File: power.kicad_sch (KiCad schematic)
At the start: 13 parts, among them J1 Conn_01x02_Socket, U1 TPS61170DRVR

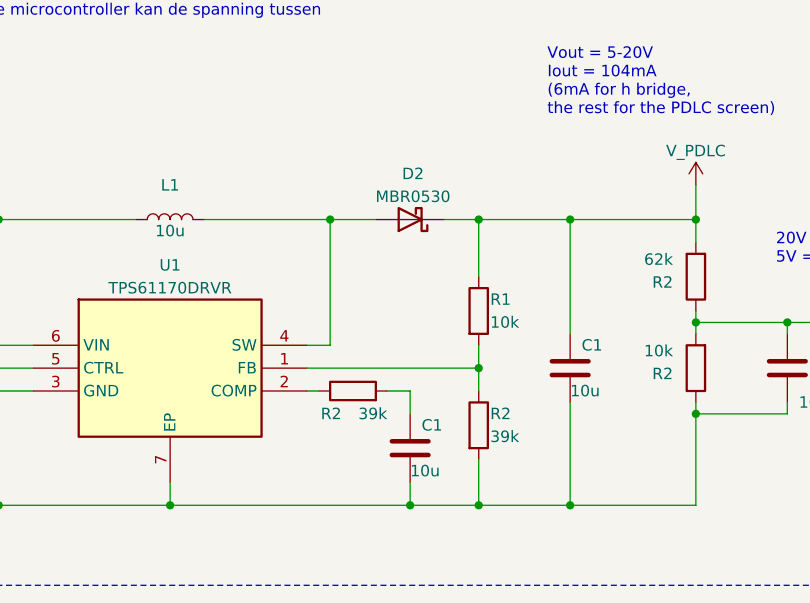
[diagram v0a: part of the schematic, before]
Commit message: Buffed the diode, changed compensation components
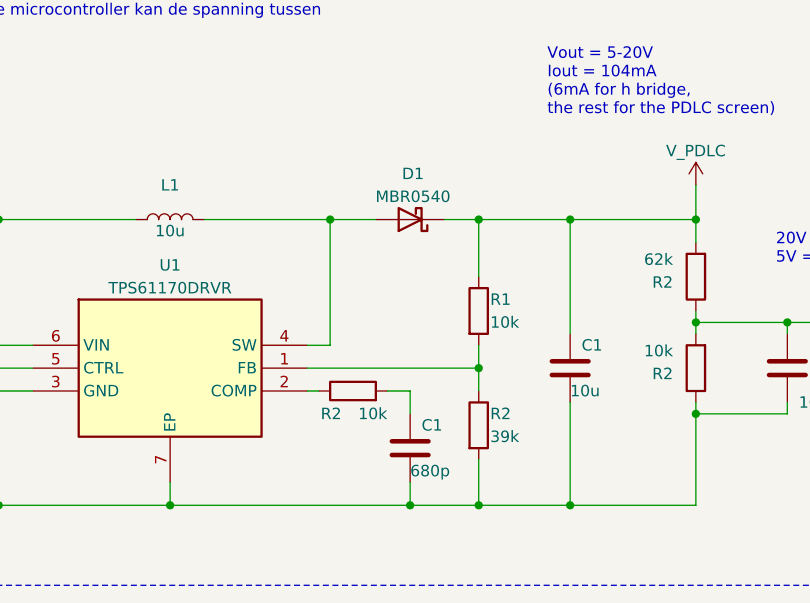
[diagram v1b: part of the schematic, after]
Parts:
- removed D2: MBR0530, Diode_SMD:D_SOD-123, symbol Diode:MBR0530
- added D1: MBR0540, Diode_SMD:D_SOD-123, symbol Diode:MBR0540
- C1: value 10u -> 680p
- R2: value 39k -> 10k
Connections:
- net VCC: now also D1.1 (K)
- net at L1.1, U1.4 (SW): now also D1.2 (A)
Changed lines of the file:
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@@
       (effects (font (size 1.27 1.27)) (justify left))
     )
-    (property "Value" "39k" (at 217.17 69.85 90)
+    (property "Value" "10k" (at 217.17 69.85 90)
       (effects (font (size 1.27 1.27)) (justify left))
     )
@@
       (effects (font (size 1.27 1.27)) (justify left))
     )
-    (property "Value" "10u" (at 219.71 76.2 0)
+    (property "Value" "680p" (at 219.71 76.2 0)
       (effects (font (size 1.27 1.27)) (justify left))
     )
@@
     )
   )
-  (symbol (lib_id "Diode:MBR0530") (at 219.71 48.26 180) (unit 1)
-    (in_bom yes) (on_board yes) (dnp no) (fields_autoplaced)
-    (property "Reference" "D2" (at 220.0275 43.18 0)
-      (effects (font (size 1.27 1.27)))
-    )
-    (property "Value" "MBR0530" (at 220.0275 45.72 0)
+  (symbol (lib_id "Diode:MBR0540") (at 219.71 48.26 180) (unit 1)
+    (in_bom yes) (on_board yes) (dnp no) (fields_autoplaced)
+    (property "Reference" "D1" (at 220.0275 43.18 0)
+      (effects (font (size 1.27 1.27)))
+    )
+    (property "Value" "MBR0540" (at 220.0275 45.72 0)
       (effects (font (size 1.27 1.27)))
     )
@@
       (project "RookBril"
         (path "/5dc439a9-720d-4bdc-b61f-78a76fde4df5/2d26b15a-54d8-4f7d-a410-dc25ffe321a1"
-          (reference "D2") (unit 1)
-        )
-      )
+          (reference "D1") (unit 1)
+        )
+      )

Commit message: updated schematic
alles toegevoegd aan de schematic
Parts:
- removed J1: Conn_01x02_Socket, symbol Connector:Conn_01x02_Socket
- renumbered C1 to C?, L1 to L?, R2 to R?, R1 to R?, U1 to U3
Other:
- note removed: "0.8-1.5V/cell 3 cell 2.4-4.5V totaal"
- note removed: "3V Buck-Boost"
- note removed: "Een simpele ldo is niet goed want dat zorgt ervoor dat de pwm voltage niet constant blijft en daardoor is de pdlc output voltage niet constant"
- moved on the sheet: C?, D1, L?, R?, U3

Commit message: footprint assignments gedaan + verbeteringen
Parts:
- removed L?: 10u, symbol Device:L
- added L1: VLCF5020T-100M1R1-1, VLCF5020, symbol SamacSys_Parts:VLCF5020T-100M1R1-1
- C? (x4): footprint (none) -> Capacitor_SMD:C_0805_2012Metric_Pad1.18x1.45mm_HandSolder
- renumbered U3 to U2
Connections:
- net +BATT: now also L1.1
- net at D1.2 (A), U2.4 (SW): now also L1.2
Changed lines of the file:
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@@
   (junction (at 206.375 107.315) (diameter 0) (color 0 0 0 0)
   )
+  (junction (at 155.575 95.885) (diameter 0) (color 0 0 0 0)
+  )
   (junction (at 196.215 117.475) (diameter 0) (color 0 0 0 0)
   )
@@
   )
   (junction (at 196.215 95.885) (diameter 0) (color 0 0 0 0)
-  )
-  (junction (at 155.575 95.885) (diameter 0) (color 0 0 0 0)
   )
   (junction (at 172.085 95.885) (diameter 0) (color 0 0 0 0)
@@
     (stroke (width 0) (type dash))
   )
-  (wire (pts (xy 141.605 95.885) (xy 155.575 95.885))
-    (stroke (width 0) (type default))
-  )
-  (wire (pts (xy 118.745 95.885) (xy 133.985 95.885))
-    (stroke (width 0) (type default))
-  )
   (wire (pts (xy 172.085 112.395) (xy 172.085 114.935))
     (stroke (width 0) (type default))
@@
     (stroke (width 0) (type dash))
   )
+  (wire (pts (xy 118.745 95.885) (xy 127 95.885))
+    (stroke (width 0) (type default))
+  )
   (wire (pts (xy 155.575 95.885) (xy 155.575 109.855))
     (stroke (width 0) (type default))
@@
   )
   (wire (pts (xy 164.465 127.635) (xy 172.085 127.635))
+    (stroke (width 0) (type default))
+  )
+  (wire (pts (xy 147.32 95.885) (xy 155.575 95.885))
     (stroke (width 0) (type default))
   )
@@
         )
         (path "/5dc439a9-720d-4bdc-b61f-78a76fde4df5/2d26b15a-54d8-4f7d-a410-dc25ffe321a1"
-          (reference "R8") (unit 1)
+          (reference "R12") (unit 1)
         )
       )
@@
       (effects (font (size 1.27 1.27)) (justify left))
     )
-    (property "Footprint" "" (at 183.2102 116.205 0)
+    (property "Footprint" "Capacitor_SMD:C_0805_2012Metric_Pad1.18x1.45mm_HandSolder" (at 183.2102 116.205 0)
       (effects (font (size 1.27 1.27)) hide)
     )
@@
         )
         (path "/5dc439a9-720d-4bdc-b61f-78a76fde4df5/2d26b15a-54d8-4f7d-a410-dc25ffe321a1"
-          (reference "C11") (unit 1)
+          (reference "C7") (unit 1)
         )
       )
@@
   (symbol (lib_id "CustomSymbols:V_PDLC") (at 196.215 92.075 0) (unit 1)
     (in_bom yes) (on_board yes) (dnp no) (fields_autoplaced)
-    (property "Reference" "#PWR036" (at 196.215 95.885 0)
+    (property "Reference" "#PWR027" (at 196.215 95.885 0)
       (effects (font (size 1.27 1.27)) hide)
     )
@@
       (project "RookBril"
         (path "/5dc439a9-720d-4bdc-b61f-78a76fde4df5/2d26b15a-54d8-4f7d-a410-dc25ffe321a1"
-          (reference "#PWR036") (unit 1)
-        )
-      )
-    )
-  )
-  (symbol (lib_id "Device:L") (at 137.795 95.885 270) (mirror x) (unit 1)
-    (in_bom yes) (on_board yes) (dnp no)
-    (property "Reference" "L?" (at 137.795 92.075 90)
-      (effects (font (size 1.27 1.27)))
-    )
-    (property "Value" "10u" (at 137.795 97.155 90)
-      (effects (font (size 1.27 1.27)))
-    )
-    (property "Footprint" "" (at 137.795 95.885 0)
-      (effects (font (size 1.27 1.27)) hide)
-    )
-    (property "Datasheet" "~" (at 137.795 95.885 0)
-      (effects (font (size 1.27 1.27)) hide)
-    )
-    (pin "1")
-    (pin "2")
-    (instances
-      (project "RookBril"
-        (path "/5dc439a9-720d-4bdc-b61f-78a76fde4df5"
-          (reference "L?") (unit 1)
-        )
-        (path "/5dc439a9-720d-4bdc-b61f-78a76fde4df5/2d26b15a-54d8-4f7d-a410-dc25ffe321a1"
-          (reference "L1") (unit 1)
+          (reference "#PWR027") (unit 1)
         )
       )
@@
   (symbol (lib_id "power:GND") (at 102.235 128.905 0) (unit 1)
     (in_bom yes) (on_board yes) (dnp no) (fields_autoplaced)
-    (property "Reference" "#PWR038" (at 102.235 135.255 0)
+    (property "Reference" "#PWR029" (at 102.235 135.255 0)
       (effects (font (size 1.27 1.27)) hide)
     )
@@
       (project "RookBril"
         (path "/5dc439a9-720d-4bdc-b61f-78a76fde4df5/2d26b15a-54d8-4f7d-a410-dc25ffe321a1"
-          (reference "#PWR038") (unit 1)
+          (reference "#PWR029") (unit 1)
         )
       )
@@
         )
         (path "/5dc439a9-720d-4bdc-b61f-78a76fde4df5/2d26b15a-54d8-4f7d-a410-dc25ffe321a1"
-          (reference "R4") (unit 1)
+          (reference "R8") (unit 1)
         )
       )
@@
       (effects (font (size 1.27 1.27)) (justify left))
     )
-    (property "Footprint" "" (at 103.2002 113.665 0)
+    (property "Footprint" "Capacitor_SMD:C_0805_2012Metric_Pad1.18x1.45mm_HandSolder" (at 103.2002 113.665 0)
       (effects (font (size 1.27 1.27)) hide)
     )
@@
         )
         (path "/5dc439a9-720d-4bdc-b61f-78a76fde4df5/2d26b15a-54d8-4f7d-a410-dc25ffe321a1"
-          (reference "C10") (unit 1)
+          (reference "C6") (unit 1)
         )
       )
@@
         )
         (path "/5dc439a9-720d-4bdc-b61f-78a76fde4df5/2d26b15a-54d8-4f7d-a410-dc25ffe321a1"
-          (reference "R7") (unit 1)
+          (reference "R11") (unit 1)
         )
       )
@@
   (symbol (lib_id "power:+BATT") (at 102.235 93.345 0) (unit 1)
     (in_bom yes) (on_board yes) (dnp no) (fields_autoplaced)
-    (property "Reference" "#PWR037" (at 102.235 97.155 0)
+    (property "Reference" "#PWR028" (at 102.235 97.155 0)
       (effects (font (size 1.27 1.27)) hide)
     )
@@
       (project "RookBril"
         (path "/5dc439a9-720d-4bdc-b61f-78a76fde4df5/2d26b15a-54d8-4f7d-a410-dc25ffe321a1"
-          (reference "#PWR037") (unit 1)
+          (reference "#PWR028") (unit 1)
         )
       )
@@
         )
         (path "/5dc439a9-720d-4bdc-b61f-78a76fde4df5/2d26b15a-54d8-4f7d-a410-dc25ffe321a1"
-          (reference "R6") (unit 1)
+          (reference "R10") (unit 1)
         )
       )
@@
       (effects (font (size 1.27 1.27)) (justify left))
     )
-    (property "Footprint" "" (at 207.3402 116.205 0)
+    (property "Footprint" "Capacitor_SMD:C_0805_2012Metric_Pad1.18x1.45mm_HandSolder" (at 207.3402 116.205 0)
       (effects (font (size 1.27 1.27)) hide)
     )
@@
         )
         (path "/5dc439a9-720d-4bdc-b61f-78a76fde4df5/2d26b15a-54d8-4f7d-a410-dc25ffe321a1"
-          (reference "C12") (unit 1)
+          (reference "C8") (unit 1)
         )
       )
@@
         )
         (path "/5dc439a9-720d-4bdc-b61f-78a76fde4df5/2d26b15a-54d8-4f7d-a410-dc25ffe321a1"
-          (reference "R5") (unit 1)
+          (reference "R9") (unit 1)
         )
       )
@@
       (effects (font (size 1.27 1.27)) (justify left))
     )
-    (property "Footprint" "" (at 165.4302 125.095 0)
+    (property "Footprint" "Capacitor_SMD:C_0805_2012Metric_Pad1.18x1.45mm_HandSolder" (at 165.4302 125.095 0)
       (effects (font (size 1.27 1.27)) hide)
     )
@@
         )
         (path "/5dc439a9-720d-4bdc-b61f-78a76fde4df5/2d26b15a-54d8-4f7d-a410-dc25ffe321a1"
-          (reference "C13") (unit 1)
+          (reference "C9") (unit 1)
         )
       )
@@
     )
   )
+  (symbol (lib_id "SamacSys_Parts:VLCF5020T-100M1R1-1") (at 127 95.885 0) (unit 1)
+    (in_bom yes) (on_board yes) (dnp no) (fields_autoplaced)
+    (property "Reference" "L1" (at 137.16 90.17 0)
+      (effects (font (size 1.27 1.27)))
+    )
+    (property "Value" "VLCF5020T-100M1R1-1" (at 137.16 92.71 0)
+      (effects (font (size 1.27 1.27)))
+    )
+    (property "Footprint" "VLCF5020" (at 143.51 94.615 0)
+      (effects (font (size 1.27 1.27)) (justify left) hide)
+    )
+    (property "Datasheet" "https://product.tdk.com/system/files/dam/doc/product/inductor/inductor/smd/catalog/inductor_commercial_power_vlcf5020-1_en.pdf" (at 143.51 97.155 0)
+      (effects (font (size 1.27 1.27)) (justify left) hide)
+    )
+    (property "Description" "TDK VLC5020 Series Shielded Wire-wound SMD Inductor 10 uH +/-20% 1.5A Idc" (at 143.51 99.695 0)
+      (effects (font (size 1.27 1.27)) (justify left) hide)
+    )
+    (property "Height" "" (at 143.51 102.235 0)
+      (effects (font (size 1.27 1.27)) (justify left) hide)
+    )
+    (property "Mouser Part Number" "810-VLCF52T100M1R11" (at 143.51 104.775 0)
+      (effects (font (size 1.27 1.27)) (justify left) hide)
+    )
+    (property "Mouser Price/Stock" "https://www.mouser.co.uk/ProductDetail/TDK/VLCF5020T-100M1R1-1?qs=O2qRfqcg9D93TlFS8ggxKg%3D%3D" (at 143.51 107.315 0)
+      (effects (font (size 1.27 1.27)) (justify left) hide)
+    )
+    (property "Manufacturer_Name" "TDK" (at 143.51 109.855 0)
+      (effects (font (size 1.27 1.27)) (justify left) hide)
+    )
+    (property "Manufacturer_Part_Number" "VLCF5020T-100M1R1-1" (at 143.51 112.395 0)
+      (effects (font (size 1.27 1.27)) (justify left) hide)
+    )
+    (pin "1")
+    (pin "2")
+    (instances
+      (project "RookBril"
+        (path "/5dc439a9-720d-4bdc-b61f-78a76fde4df5/2d26b15a-54d8-4f7d-a410-dc25ffe321a1"
+          (reference "L1") (unit 1)
+        )
+      )
+    )
+  )
   (symbol (lib_id "CustomSymbols:TPS61170DRVR") (at 122.555 107.315 0) (unit 1)
     (in_bom yes) (on_board yes) (dnp no) (fields_autoplaced)
-    (property "Reference" "U3" (at 137.795 100.965 0)
+    (property "Reference" "U2" (at 137.795 100.965 0)
       (effects (font (size 1.27 1.27)))
     )
@@
       (project "RookBril"
         (path "/5dc439a9-720d-4bdc-b61f-78a76fde4df5/2d26b15a-54d8-4f7d-a410-dc25ffe321a1"
-          (reference "U3") (unit 1)
-        )
-      )
+          (reference "U2") (unit 1)
+        )
+      )

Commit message: aantal componenten veranderd.
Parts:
- removed L1: VLCF5020T-100M1R1-1, VLCF5020, symbol SamacSys_Parts:VLCF5020T-100M1R1-1
- added L1: VLCF5020T-100M1R1-1, Components:VLCF5020, symbol CustomSymbols:VLCF5020T-100M1R1-1
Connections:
- net +BATT: now also L1.1
- net at D1.2 (A), U2.4 (SW): now also L1.2

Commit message: nieuwe layout
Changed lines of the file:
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@@
     (effects (font (size 1.27 1.27)) (justify left bottom))
   )
-  (text "Vin_min = 3.2V\nVin_max = 6V" (at 113.665 84.455 0)
+  (text "Vin_min = 3.2V\nVin_max = 6V" (at 113.792 84.582 0)
     (effects (font (size 1.27 1.27)) (justify right bottom))
   )

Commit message: NieuwePDLCVoedingen
-LT1308
-LT3759
-Mixed schematic
-Mixed footprints
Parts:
- added C001, C19: 680p, symbol Device:C
- added C1301, C25: 100n, symbol Device:C
- added C26: 33u, symbol Device:C_Polarized
- added C27: 22n, symbol Device:C
- added C28, C3701: 50n, symbol Device:C
- added C29, C3702: 4.7u, symbol Device:C
- added C30: 10u, symbol Device:C
- added D01, D1301, D1302, D2, D3, D4, D5: ~, symbol CustomSymbols:MBRS140
- added L001, L3, L4: 4.7u, symbol Device:L
- added Q01, Q02, Q03, Q04, Q1, Q2, Q3, Q371, Q4, Q5, Q6, Q7, Q8, Q9: NMOS, symbol Simulation_SPICE:NMOS
- added R009, R30: 590k, symbol Device:R
- added R010, R19, R35: 47.6k, symbol Device:R
- added R011, R21, R31: 160k, symbol Device:R
- added R012, R22, R32: 80k, symbol Device:R
- added R013, R23, R33: 40k, symbol Device:R
- added R014, R24, R34: 20k, symbol Device:R
- added R1301, R1304 (x2), R3704, R3705, R3707: 0, symbol Device:R
- added R1302, R18, R27, R3701, R3706: 100k, symbol Device:R
- added R1303, R3703: 10k, symbol Device:R
- added R20: 300k, symbol Device:R
- added R25, R36: 5m, symbol Device:R
- added R26: 41.2k, symbol Device:R
- added R28: 118k, symbol Device:R
- added R29: 105k, symbol Device:R
- added U5: ~, symbol CustomSymbols:LT1308BCS8
- added U6: ~, symbol CustomSymbols:LT3759
- added U7: ~, symbol CustomSymbols:MixLT1308+LT3759
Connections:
- net +BATT: now also L3.1, L4.1, R29.1, U5.3 (SHDN), U5.6 (Vin), U6.11 (Vin)
- net GND: now also C001.2, C19.2, C26.2, C27.1, C28.1, C29.1, C30.1, C3701.1, C3702.1, Q01.3 (S), Q02.3 (S), Q03.3 (S), Q04.3 (S), Q1.3 (S), Q2.3 (S), Q3.3 (S), Q4.3 (S), Q6.3 (S), Q7.3 (S), Q8.3 (S), Q9.3 (S), R010.1, R1303.1, R19.1, R25.1, R26.2, R28.2, R35.1, R36.1, R3701.1, R3703.2, R3706.1, U5.4 (GND), U6.13 (GND), U7.15 (GND), U7.7 (X/GND)
- net vout_fb: now also C26.1, D4.1 (K), D5.1 (K), R20.2, R30.2, U6.10 (DRIVE)
- new net: C28.2, U6.3 (SS)
- new net: Q8.1 (D), R33.1
- new net: R30.1, R31.2, R32.2, R33.2, R34.2, R35.2, U6.2 (FBX)
- new net: Q2.1 (D), R22.1
- new net: R19.2, R20.1, R21.2, R22.2, R23.2, R24.2, U5.2 (FB)
- new net: Q7.1 (D), R32.1
- new net: C29.2, R27.1, U6.9 (INTVcc)
- new net: C25.2, D3.1 (K), D4.2 (A)
- new net: C30.2, D2.1 (K), D3.2 (A)
- new net: Q3.1 (D), R23.1
- new net: D01.1 (K), R009.2, R3704.1
- new net: C1301.2, D01.2 (A), D1301.1 (K), R3705.2
- new net: Q9.1 (D), R34.1
- new net: D5.2 (A), L4.2, Q5.1 (D)
- new net: C3701.2, R1301.1, U7.3 (SS/FB)
- new net: R009.1, R010.2, R011.2, R012.2, R013.2, R014.2, R1301.2, U7.2 (FBX/X)
- new net: R28.1, R29.2, U6. (Vc)
- new net: Q1.1 (D), R21.1
- new net: C1301.1, D1302.2 (A), L001.1, Q371.1 (D), R3705.1, U7.8 (X/SW)
- new net: R3701.2, U7.4 (RT/X)
- new net: Q371.2 (G), R1304.1, U7.10 (GATE/Vin)
- new net: L001.2, R1304.2, U7.13 (Vin/X)
- new net: R1302.2, U7.1 (Vc/Vc)
- new net: C3702.2, U7.11 (INTVcc/X)
- new net: R3704.2, U7.12 (DRIVE/LBI)
- new net: R3707.2, U7.14 (EN-UVLO/LBO)
- new net: R1304.1, U7.5 (SYNC/SHDN)
- new net: R3706.2, U7.6 (PGOOD/X)
- new net: Q371.3 (S), R36.2, U7.9 (SENSE/X)
- new net: C25.1, D2.2 (A), L3.2, U5.5 (SW)
- new net: Q03.1 (D), R013.1
- new net: Q5.3 (S), R25.2, U6.7 (SENSE)
- new net: R26.1, U6.4 (RT)
- new net: Q04.1 (D), R014.1
- new net: Q4.1 (D), R24.1
- new net: D1301.2 (A), D1302.1 (K)
- new net: C001.1, R1302.1
- new net: R27.2, U6.6 (PGOOD)
- new net: Q6.1 (D), R31.1
- new net: C27.2, U6. (Vc)
- new net: R18.2, U5.1 (Vcc)
- new net: Q5.2 (G), U6.8 (GATE)
- new net: Q01.1 (D), R011.1
- new net: C19.1, R18.1
- new net: Q02.1 (D), R012.1
- new net pdlc_bit0: Q01.2 (G), Q1.2 (G), Q3.2 (G), Q6.2 (G)
- new net pdlc_bit1: Q02.2 (G), Q2.2 (G), Q4.2 (G), Q7.2 (G)
- new net pdlc_bit2: Q03.2 (G), Q8.2 (G)
- new net pdlc_bit3: Q04.2 (G), Q9.2 (G)
- new net vout_EN: R1303.2, R1304.2, R3703.1, R3707.1
- no-connect marks 0 -> 3
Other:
- moved on the sheet: C?, D1, L1, R?, U2

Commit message: PCBv2.01
Eerste versie van de tweede versie van de pcb prototype.
Nieuwe PDLC voeding, extra pinnen beschikbaar voor GUI inclusief voeding pinnen.
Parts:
- removed C001: 680p, symbol Device:C
- removed C1301: 100n, symbol Device:C
- removed C26: 33u, symbol Device:C_Polarized
- removed C30: 10u, symbol Device:C
- removed C3701: 50n, symbol Device:C
- removed C3702: 4.7u, symbol Device:C
- removed C? (x2): 10u, Capacitor_SMD:C_0805_2012Metric_Pad1.18x1.45mm_HandSolder, symbol Device:C
- removed C?: 100n, Capacitor_SMD:C_0805_2012Metric_Pad1.18x1.45mm_HandSolder, symbol Device:C
- removed C?: 680p, Capacitor_SMD:C_0805_2012Metric_Pad1.18x1.45mm_HandSolder, symbol Device:C
- removed D01, D1301, D1302, D4: ~, symbol CustomSymbols:MBRS140
- removed D1: MBR0540, Diode_SMD:D_SOD-123, symbol Diode:MBR0540
- removed L001, L3: 4.7u, symbol Device:L
- removed L1: VLCF5020T-100M1R1-1, Components:VLCF5020, symbol CustomSymbols:VLCF5020T-100M1R1-1
- removed Q01, Q02, Q03, Q04, Q1, Q2, Q3, Q371, Q4: NMOS, symbol Simulation_SPICE:NMOS
- removed R009: 590k, symbol Device:R
- removed R010, R19: 47.6k, symbol Device:R
- removed R011, R21: 160k, symbol Device:R
- removed R012, R22: 80k, symbol Device:R
- removed R013, R23: 40k, symbol Device:R
- removed R014, R24: 20k, symbol Device:R
- removed R1301, R1304 (x2), R3704, R3705, R3707: 0, symbol Device:R
- removed R1302, R18, R3701, R3706: 100k, symbol Device:R
- removed R1303, R3703: 10k, symbol Device:R
- removed R20: 300k, symbol Device:R
- removed R29: 105k, symbol Device:R
- removed R36: 5m, symbol Device:R
- removed R?: 39k, Resistor_SMD:R_0805_2012Metric_Pad1.20x1.40mm_HandSolder, symbol Device:R
- removed R?: 62k, Resistor_SMD:R_0805_2012Metric_Pad1.20x1.40mm_HandSolder, symbol Device:R
- removed R? (x3): 10k, Resistor_SMD:R_0805_2012Metric_Pad1.20x1.40mm_HandSolder, symbol Device:R
- removed U2: TPS61170DRVR, Components:SON65P200X200X80-7N, symbol CustomSymbols:TPS61170DRVR
- removed U5: ~, symbol CustomSymbols:LT1308BCS8
- removed U7: ~, symbol CustomSymbols:MixLT1308+LT3759
- added C10, C26, C27: 10u, Capacitor_SMD:C_0805_2012Metric_Pad1.18x1.45mm_HandSolder, symbol Device:C
- added C28: 100n, Capacitor_SMD:C_0805_2012Metric_Pad1.18x1.45mm_HandSolder, symbol Device:C
- added R11: 7.5k, Resistor_SMD:R_0805_2012Metric_Pad1.20x1.40mm_HandSolder, symbol Device:R
- C19: value 680p -> 10u; footprint (none) -> Capacitor_SMD:C_0805_2012Metric_Pad1.18x1.45mm_HandSolder
- C25: value 100n -> 10u; footprint (none) -> Capacitor_SMD:C_0805_2012Metric_Pad1.18x1.45mm_HandSolder
- C7: renamed from C29; footprint (none) -> Capacitor_SMD:C_0805_2012Metric_Pad1.18x1.45mm_HandSolder
- C8: renamed from C28; footprint (none) -> Capacitor_SMD:C_0805_2012Metric_Pad1.18x1.45mm_HandSolder
- C9: renamed from C27; footprint (none) -> Capacitor_SMD:C_0805_2012Metric_Pad1.18x1.45mm_HandSolder
- D1: renamed from D5; footprint (none) -> Diode_SMD:D_SOD-123F
- D2, D3: footprint (none) -> Diode_SMD:D_SOD-123F
- L1: renamed from L4; value 4.7u -> 10u; footprint (none) -> Components:MRS8030T100
- Q1: renamed from Q5; footprint (none) -> Package_TO_SOT_SMD:SOT-23
- Q2: renamed from Q6; footprint (none) -> Package_TO_SOT_SMD:SOT-23
- Q3: renamed from Q7; footprint (none) -> Package_TO_SOT_SMD:SOT-23
- Q4: renamed from Q8; footprint (none) -> Package_TO_SOT_SMD:SOT-23
- Q5: renamed from Q9; footprint (none) -> Package_TO_SOT_SMD:SOT-23
- R10: renamed from R27; footprint (none) -> Resistor_SMD:R_0805_2012Metric_Pad1.20x1.40mm_HandSolder
- R12: renamed from R25; footprint (none) -> Resistor_SMD:R_2010_5025Metric_Pad1.40x2.65mm_HandSolder
- R18: renamed from R30; footprint (none) -> Resistor_SMD:R_0805_2012Metric_Pad1.20x1.40mm_HandSolder
- R19: renamed from R35; footprint (none) -> Resistor_SMD:R_0805_2012Metric_Pad1.20x1.40mm_HandSolder
- R20: renamed from R31; footprint (none) -> Resistor_SMD:R_0805_2012Metric_Pad1.20x1.40mm_HandSolder
- R21: renamed from R32; footprint (none) -> Resistor_SMD:R_0805_2012Metric_Pad1.20x1.40mm_HandSolder
- R22: renamed from R33; footprint (none) -> Resistor_SMD:R_0805_2012Metric_Pad1.20x1.40mm_HandSolder
- R23: renamed from R34; footprint (none) -> Resistor_SMD:R_0805_2012Metric_Pad1.20x1.40mm_HandSolder
- R8: renamed from R28; footprint (none) -> Resistor_SMD:R_0805_2012Metric_Pad1.20x1.40mm_HandSolder
- R9: renamed from R26; footprint (none) -> Resistor_SMD:R_0805_2012Metric_Pad1.20x1.40mm_HandSolder
- U2: renamed from U6; footprint (none) -> Components:LT3759
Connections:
- net GND: now also C19.1, C25.1, C10.1, C26.1, C27.1; no longer C19.2
- net VCC: now also C19.2, C25.2, D3.1 (K), R18.2, U2.10 (DRIVE), C10.2, C26.2
- net vout_EN: now also R8.1, U2.12 (EN/UVLO)
- net at D2.1 (K), D3.2 (A): now also C28.1
- net at D1.2 (A), L1.2, Q1.1 (D): now also C28.2
- net at D2.2 (A): now also D1.1 (K), C27.2; no longer C25.1
- net at C9.2: now also R11.1; no longer U2. (Vc)
- removed net vout_fb: D1.1 (K), R18.2, U2.10 (DRIVE)
- new net: R11.2, U2.1 (Vc)
- no-connect marks 3 -> 1
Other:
- moved on the sheet: C7, C8, C9, D1, L1, Q1, Q2, Q3, Q4, Q5, R10, R12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
